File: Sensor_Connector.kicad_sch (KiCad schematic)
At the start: 5 parts, among them J6 Sensor_Conn

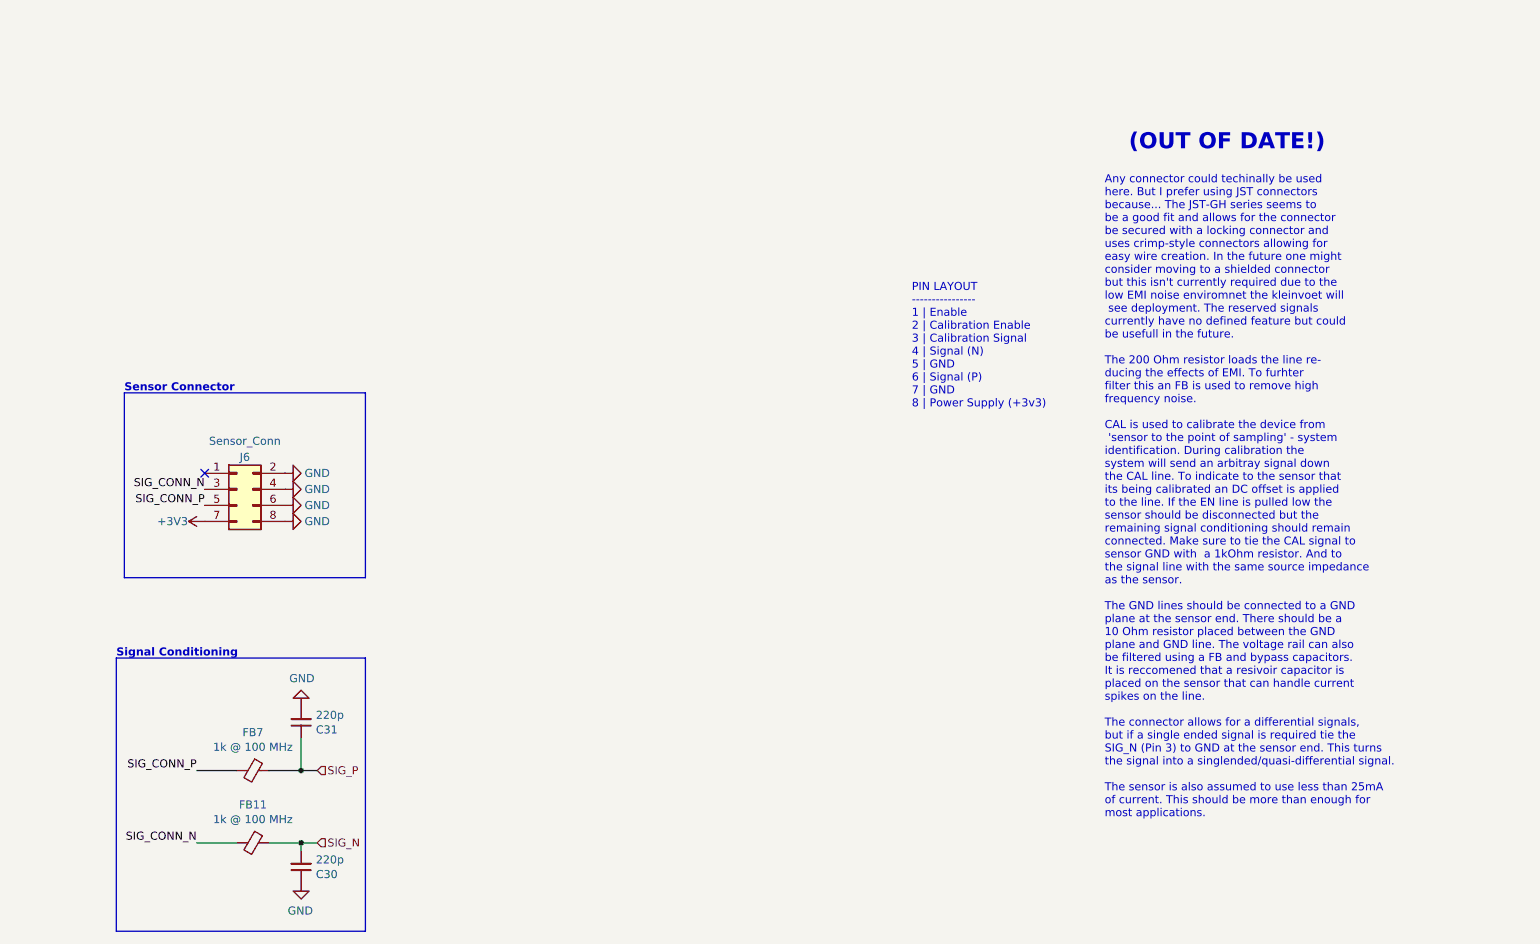
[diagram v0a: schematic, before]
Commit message: (deps) upgrade to KiCad 7.0
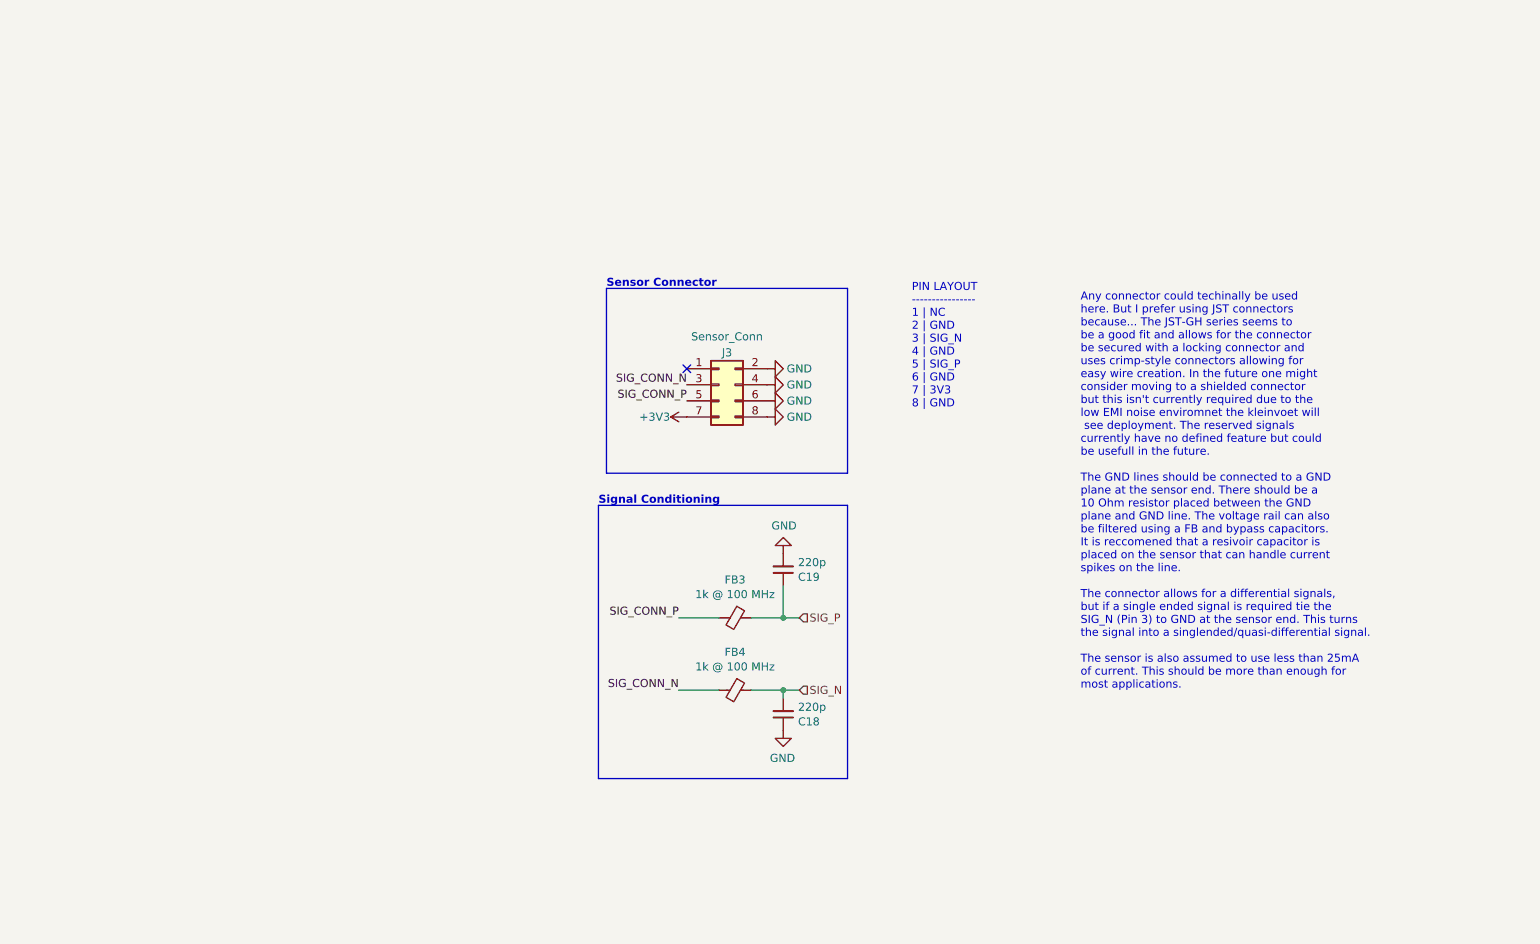
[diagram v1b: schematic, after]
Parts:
- renumbered C30 to C18, C31 to C19, FB7 to FB3, FB11 to FB4, J6 to J3
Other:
- note added: "PIN LAYOUT ---------------- 1 | NC 2 | GND 3 | SIG_N 4 | GND 5 | SIG_P 6 | GND 7 | 3V3 8 | GND"
- note removed: "(OUT OF DATE!)"
- note removed: "PIN LAYOUT ---------------- 1 | Enable 2 | Calibration Enable 3 | Calibration Signal 4 | Signal (N) 5 | GND 6 | Signal (P) 7 | GND 8 | Power Supply (+3v3)"
- moved on the sheet: C18, C19, FB3, FB4, J3

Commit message: (sch) new sensor connector interface
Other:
- note added: "NEW CONNECTOR INTERFACE"
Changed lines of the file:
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@@
     (effects (font (size 1.27 1.27) (thickness 0.254) bold) (justify left bottom))
+  )
+  (text "NEW CONNECTOR INTERFACE" (at 62.865 68.58 0)
+    (effects (font (size 1.27 1.27)) (justify left bottom))
   )
   (text "Signal Conditioning" (at 109.22 92.71 0)
     (effects (font (size 1.27 1.27) (thickness 0.254) bold) (justify left bottom))
   )
+  (label "SIG_CONN_P" (at 84.455 55.88 0) (fields_autoplaced)
+    (effects (font (size 1.27 1.27)) (justify left bottom))
+  )
   (label "SIG_CONN_P" (at 123.19 76.2 180) (fields_autoplaced)
     (effects (font (size 1.27 1.27)) (justify right bottom))
@@
     (effects (font (size 1.27 1.27)) (justify right bottom))
   )
+  (label "VCM" (at 84.455 63.5 0) (fields_autoplaced)
+    (effects (font (size 1.27 1.27)) (justify left bottom))
+  )
   (label "SIG_CONN_N" (at 121.92 121.92 180) (fields_autoplaced)
     (effects (font (size 1.27 1.27)) (justify right bottom))
+  )
+  (label "SIG_CONN_N" (at 81.915 55.88 180) (fields_autoplaced)
+    (effects (font (size 1.27 1.27)) (justify right bottom))
+  )
+  (label "3v3_ANALOG" (at 84.455 65.405 0) (fields_autoplaced)
+    (effects (font (size 1.27 1.27)) (justify left bottom))
   )
   (hierarchical_label "SIG_P" (shape input) (at 140.97 110.49 0) (fields_autoplaced)
@@
         )
       )
+    )
+  )
+  (symbol (lib_id "power:GND") (at 81.915 62.23 270) (unit 1)
+    (in_bom yes) (on_board yes) (dnp no)
+    (property "Reference" "#PWR0159" (at 75.565 62.23 0)
+      (effects (font (size 1.27 1.27)) hide)
+    )
+    (property "Value" "GND" (at 76.835 62.23 90)
+      (effects (font (size 1.27 1.27)))
+    )
+    (property "Footprint" "" (at 81.915 62.23 0)
+      (effects (font (size 1.27 1.27)) hide)
+    )
+    (property "Datasheet" "" (at 81.915 62.23 0)
+      (effects (font (size 1.27 1.27)) hide)
+    )
+    (pin "1")
+    (instances
+      (project "kleinvoet"
+        (path "/4185c36c-c66e-4dbd-be5d-841e551f4885/00000000-0000-0000-0000-00005ee5ecad/00000000-0000-0000-0000-00005ee62c2b"
+          (reference "#PWR0159") (unit 1)
+        )
+        (path "/4185c36c-c66e-4dbd-be5d-841e551f4885/00000000-0000-0000-0000-00005ee5ecad/00000000-0000-0000-0000-00005eff6d57"
+          (reference "#PWR0168") (unit 1)
+        )
+      )
+    )
+  )
+  (symbol (lib_id "power:GND") (at 81.915 65.405 270) (mirror x) (unit 1)
+    (in_bom yes) (on_board yes) (dnp no)
+    (property "Reference" "#PWR0162" (at 75.565 65.405 0)
+      (effects (font (size 1.27 1.27)) hide)
+    )
+    (property "Value" "GND" (at 76.835 65.405 90)
+      (effects (font (size 1.27 1.27)))
+    )
+    (property "Footprint" "" (at 81.915 65.405 0)
+      (effects (font (size 1.27 1.27)) hide)
+    )
+    (property "Datasheet" "" (at 81.915 65.405 0)
+      (effects (font (size 1.27 1.27)) hide)
+    )
+    (pin "1")
+    (instances
+      (project "kleinvoet"
+        (path "/4185c36c-c66e-4dbd-be5d-841e551f4885/00000000-0000-0000-0000-00005ee5ecad/00000000-0000-0000-0000-00005ee62c2b"
+          (reference "#PWR0162") (unit 1)
+        )
+        (path "/4185c36c-c66e-4dbd-be5d-841e551f4885/00000000-0000-0000-0000-00005ee5ecad/00000000-0000-0000-0000-00005eff6d57"
+          (reference "#PWR0169") (unit 1)
+        )
+      )
+    )
+  )
+  (symbol (lib_id "power:GND") (at 84.455 59.69 90) (unit 1)
+    (in_bom yes) (on_board yes) (dnp no)
+    (property "Reference" "#PWR0158" (at 90.805 59.69 0)
+      (effects (font (size 1.27 1.27)) hide)
+    )
+    (property "Value" "GND" (at 89.535 59.69 90)
+      (effects (font (size 1.27 1.27)))
+    )
+    (property "Footprint" "" (at 84.455 59.69 0)
+      (effects (font (size 1.27 1.27)) hide)
+    )
+    (property "Datasheet" "" (at 84.455 59.69 0)
+      (effects (font (size 1.27 1.27)) hide)
+    )
+    (pin "1")
+    (instances
+      (project "kleinvoet"
+        (path "/4185c36c-c66e-4dbd-be5d-841e551f4885/00000000-0000-0000-0000-00005ee5ecad/00000000-0000-0000-0000-00005ee62c2b"
+          (reference "#PWR0158") (unit 1)
+        )
+        (path "/4185c36c-c66e-4dbd-be5d-841e551f4885/00000000-0000-0000-0000-00005ee5ecad/00000000-0000-0000-0000-00005eff6d57"
+          (reference "#PWR0166") (unit 1)
+        )
+      )
+    )
+  )
+  (symbol (lib_id "power:GND") (at 81.915 59.69 270) (mirror x) (unit 1)
+    (in_bom yes) (on_board yes) (dnp no)
+    (property "Reference" "#PWR0152" (at 75.565 59.69 0)
+      (effects (font (size 1.27 1.27)) hide)
+    )
+    (property "Value" "GND" (at 76.835 59.69 90)
+      (effects (font (size 1.27 1.27)))
+    )
+    (property "Footprint" "" (at 81.915 59.69 0)
+      (effects (font (size 1.27 1.27)) hide)
+    )
+    (property "Datasheet" "" (at 81.915 59.69 0)
+      (effects (font (size 1.27 1.27)) hide)
+    )
+    (pin "1")
+    (instances
+      (project "kleinvoet"
+        (path "/4185c36c-c66e-4dbd-be5d-841e551f4885/00000000-0000-0000-0000-00005ee5ecad/00000000-0000-0000-0000-00005ee62c2b"
+          (reference "#PWR0152") (unit 1)
+        )
+        (path "/4185c36c-c66e-4dbd-be5d-841e551f4885/00000000-0000-0000-0000-00005ee5ecad/00000000-0000-0000-0000-00005eff6d57"
+          (reference "#PWR0164") (unit 1)
+        )
+      )

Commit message: (sch) plan board detect
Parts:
- added R56: OPEN, Resistor_SMD:R_0603_1608Metric_Pad0.98x0.95mm_HandSolder, symbol Device:R_Small
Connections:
- net SIG_N: now also R56.2
- net SIG_P: now also R56.1
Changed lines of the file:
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@@
+    (stroke (width 0) (type default))
+  )
+  (wire (pts (xy 138.43 110.49) (xy 138.43 113.03))
     (stroke (width 0) (type default))
   )
@@
   )
   (polyline (pts (xy 148.59 135.89) (xy 148.59 92.71))
+    (stroke (width 0) (type default))
+  )
+  (wire (pts (xy 138.43 118.11) (xy 138.43 121.92))
     (stroke (width 0) (type default))
   )
@@
         )
       )
+    )
+  )
+  (symbol (lib_id "Device:R_Small") (at 138.43 115.57 0) (unit 1)
+    (in_bom yes) (on_board yes) (dnp no)
+    (property "Reference" "R56" (at 142.875 115.57 90)
+      (effects (font (size 1.27 1.27)))
+    )
+    (property "Value" "OPEN" (at 140.97 115.57 90)
+      (effects (font (size 1.27 1.27)))
+    )
+    (property "Footprint" "Resistor_SMD:R_0603_1608Metric_Pad0.98x0.95mm_HandSolder" (at 138.43 115.57 0)
+      (effects (font (size 1.27 1.27)) hide)
+    )
+    (property "Datasheet" "~" (at 138.43 115.57 0)
+      (effects (font (size 1.27 1.27)) hide)
+    )
+    (property "MPN" "DNP" (at 138.43 115.57 0)
+      (effects (font (size 1.27 1.27)) hide)
+    )
+    (property "Mfr." "DNP" (at 138.43 115.57 0)
+      (effects (font (size 1.27 1.27)) hide)
+    )
+    (pin "1")
+    (pin "2")
+    (instances
+      (project "kleinvoet"
+        (path "/4185c36c-c66e-4dbd-be5d-841e551f4885/00000000-0000-0000-0000-00005ee5ecad/00000000-0000-0000-0000-00005ee62baf"
+          (reference "R56") (unit 1)
+        )
+        (path "/4185c36c-c66e-4dbd-be5d-841e551f4885/00000000-0000-0000-0000-00005ee5ecad/00000000-0000-0000-0000-00005ee91c90"
+          (reference "R57") (unit 1)
+        )
+        (path "/4185c36c-c66e-4dbd-be5d-841e551f4885/00000000-0000-0000-0000-00005ee5ecad/00000000-0000-0000-0000-00005ee62c2b"
+          (reference "R56") (unit 1)
+        )
+        (path "/4185c36c-c66e-4dbd-be5d-841e551f4885/00000000-0000-0000-0000-00005ee5ecad/00000000-0000-0000-0000-00005eff6d57"
+          (reference "R57") (unit 1)
+        )
+      )

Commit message: (sch) relabel
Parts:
- renumbered C19 to C501, C18 to C502, FB3 to FB501, FB4 to FB502, J3 to J501

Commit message: (bc) finish up ERC
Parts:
- removed FB501, FB502: 1k @ 100 MHz, Inductor_SMD:L_0603_1608Metric_Pad1.05x0.95mm_HandSolder, symbol Device:Ferrite_Bead_Small
- added FB501, FB503: 1k@100MHz, Inductor_SMD:L_0603_1608Metric_Pad1.05x0.95mm_HandSolder, symbol Device:FerriteBead_Small
- R56: now not fitted; now left out of the parts list
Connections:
- net +3V3 is gone; now on net GND: J501.7 (Pin_7)
- net GND: now also J501.5 (Pin_5); no longer J501.2 (Pin_2), J501.4 (Pin_4), J501.6 (Pin_6), J501.8 (Pin_8)
- net SIG_CONN_N: now also J501.1 (Pin_1), FB501.1; no longer J501.3 (Pin_3)
- net SIG_CONN_P: now also J501.2 (Pin_2), FB503.1; no longer J501.5 (Pin_5)
- net SIG_N: now also FB501.2
- net SIG_P: now also FB503.2
- new net 3v3A: J501.8 (Pin_8)
- no-connect marks 1 -> 3
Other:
- note added: "RESERVED"
- note removed: "Any connector could techinally be used here. But I prefer using JST connectors because... The JST-GH series seems to be a good fit and allows for the connector be secured with a locking connector and uses crimp-style connectors allowing for easy wire creation. In the future one might consider moving to a shielded connector but this isn't currently required due to the low EMI noise enviromnet the 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"
- note removed: "NEW CONNECTOR INTERFACE"
- note removed: "PIN LAYOUT ---------------- 1 | NC 2 | GND 3 | SIG_N 4 | GND 5 | SIG_P 6 | GND 7 | 3V3 8 | GND"
- moved on the sheet: C501, C502, J501

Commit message: (hk) asign footprints
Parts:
- renumbered FB503 to FB501, FB501 to FB502
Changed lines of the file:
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@@
         )
         (path "/4185c36c-c66e-4dbd-be5d-841e551f4885/b53619ea-788f-4bc9-9946-594014d7d22c/7d55f5f7-ad99-481b-88b5-315ad3d2b07e"
-          (reference "C1104") (unit 1)
+          (reference "C1102") (unit 1)
         )
       )
@@
         )
         (path "/4185c36c-c66e-4dbd-be5d-841e551f4885/b53619ea-788f-4bc9-9946-594014d7d22c/7d55f5f7-ad99-481b-88b5-315ad3d2b07e"
-          (reference "C1103") (unit 1)
+          (reference "C1101") (unit 1)
         )
       )
@@
   (symbol (lib_id "Device:FerriteBead_Small") (at 39.37 80.645 90) (unit 1)
     (in_bom yes) (on_board yes) (dnp no) (fields_autoplaced)
-    (property "Reference" "FB501" (at 39.3319 74.93 90)
+    (property "Reference" "FB502" (at 39.3319 74.93 90)
       (effects (font (size 1.27 1.27)))
     )
@@
       (project "kleinvoet"
         (path "/4185c36c-c66e-4dbd-be5d-841e551f4885/00000000-0000-0000-0000-00005ee5ecad/00000000-0000-0000-0000-00005ee62c2b"
-          (reference "FB501") (unit 1)
+          (reference "FB502") (unit 1)
         )
         (path "/4185c36c-c66e-4dbd-be5d-841e551f4885/00000000-0000-0000-0000-00005ee5ecad/f1c168a4-8e09-4be7-8226-fa7de49180b9"
@@
   (symbol (lib_id "Device:FerriteBead_Small") (at 39.37 69.215 90) (unit 1)
     (in_bom yes) (on_board yes) (dnp no) (fields_autoplaced)
-    (property "Reference" "FB503" (at 39.3319 63.5 90)
+    (property "Reference" "FB501" (at 39.3319 63.5 90)
       (effects (font (size 1.27 1.27)))
     )
@@
       (project "kleinvoet"
         (path "/4185c36c-c66e-4dbd-be5d-841e551f4885/00000000-0000-0000-0000-00005ee5ecad/00000000-0000-0000-0000-00005ee62c2b"
-          (reference "FB503") (unit 1)
+          (reference "FB501") (unit 1)
         )
         (path "/4185c36c-c66e-4dbd-be5d-841e551f4885/00000000-0000-0000-0000-00005ee5ecad/f1c168a4-8e09-4be7-8226-fa7de49180b9"
@@
         )
         (path "/4185c36c-c66e-4dbd-be5d-841e551f4885/b53619ea-788f-4bc9-9946-594014d7d22c/7d55f5f7-ad99-481b-88b5-315ad3d2b07e"
-          (reference "R1102") (unit 1)
+          (reference "R1101") (unit 1)
         )
       )

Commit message: (sch) change passives to 0402
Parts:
- C501, C502: footprint Capacitor_SMD:C_0603_1608Metric_Pad1.08x0.95mm_HandSolder -> Capacitor_SMD:C_0402_1005Metric; MPN C0603C221J5GACTU -> GRT1555C1H221FA02D; Mfr. KEMET -> Murata
- FB501, FB502: Mfr. (none) -> Murata
- R56: footprint Resistor_SMD:R_0603_1608Metric_Pad0.98x0.95mm_HandSolder -> Resistor_SMD:R_0402_1005Metric_Pad0.72x0.64mm_HandSolder
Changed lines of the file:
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@@
       (effects (font (size 1.27 1.27)) (justify left))
     )
-    (property "Footprint" "Capacitor_SMD:C_0603_1608Metric_Pad1.08x0.95mm_HandSolder" (at 46.99 84.455 0)
+    (property "Footprint" "Capacitor_SMD:C_0402_1005Metric" (at 46.99 84.455 0)
       (effects (font (size 1.27 1.27)) hide)
     )
@@
       (effects (font (size 1.27 1.27)) hide)
     )
-    (property "MPN" "C0603C221J5GACTU" (at 46.99 84.455 0)
+    (property "MPN" "GRT1555C1H221FA02D" (at 46.99 84.455 0)
       (effects (font (size 1.27 1.27)) hide)
     )
-    (property "Mfr." "KEMET" (at 46.99 84.455 0)
+    (property "Mfr." "Murata" (at 46.99 84.455 0)
       (effects (font (size 1.27 1.27)) hide)
     )
@@
       (effects (font (size 1.27 1.27)) (justify left))
     )
-    (property "Footprint" "Capacitor_SMD:C_0603_1608Metric_Pad1.08x0.95mm_HandSolder" (at 46.99 61.595 0)
+    (property "Footprint" "Capacitor_SMD:C_0402_1005Metric" (at 46.99 61.595 0)
       (effects (font (size 1.27 1.27)) hide)
     )
@@
       (effects (font (size 1.27 1.27)) hide)
     )
-    (property "MPN" "C0603C221J5GACTU" (at 46.99 61.595 0)
+    (property "MPN" "GRT1555C1H221FA02D" (at 46.99 61.595 0)
       (effects (font (size 1.27 1.27)) hide)
     )
-    (property "Mfr." "KEMET" (at 46.99 61.595 0)
+    (property "Mfr." "Murata" (at 46.99 61.595 0)
       (effects (font (size 1.27 1.27)) hide)
     )
@@
       (effects (font (size 1.27 1.27)) hide)
     )
+    (property "Mfr." "Murata" (at 39.37 80.645 0)
+      (effects (font (size 1.27 1.27)) hide)
+    )
     (pin "1")
     (pin "2")
@@
       (effects (font (size 1.27 1.27)) hide)
     )
+    (property "Mfr." "Murata" (at 39.37 69.215 0)
+      (effects (font (size 1.27 1.27)) hide)
+    )
     (pin "1")
     (pin "2")
@@
       (effects (font (size 1.27 1.27)))
     )
-    (property "Footprint" "Resistor_SMD:R_0603_1608Metric_Pad0.98x0.95mm_HandSolder" (at 46.99 74.295 0)
+    (property "Footprint" "Resistor_SMD:R_0402_1005Metric_Pad0.72x0.64mm_HandSolder" (at 46.99 74.295 0)
       (effects (font (size 1.27 1.27)) hide)
     )
